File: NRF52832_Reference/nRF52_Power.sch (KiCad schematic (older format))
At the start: 37 parts, among them J17 USB_B_Micro, J18 Conn_01x02_Male, U10 DW01, U11 LMV331ICT, U12 AP2138N-3.0TRG1, U13 FS8205A, U14 SLIDE_SW_DPDT, U7 TPS613222ADBVR, U8 NCV8161BSN330T1G, U9 TP4056E-SN2L1P

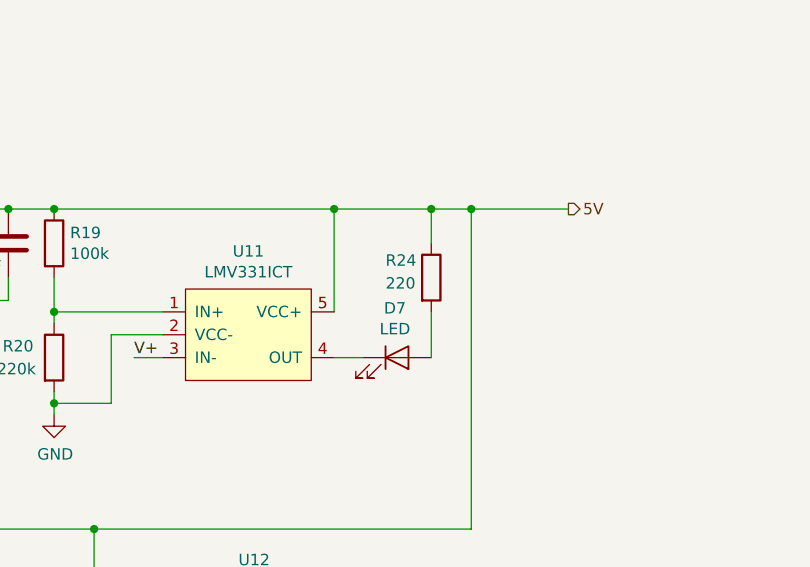
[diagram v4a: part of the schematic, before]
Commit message: Fixed wrong values for some components
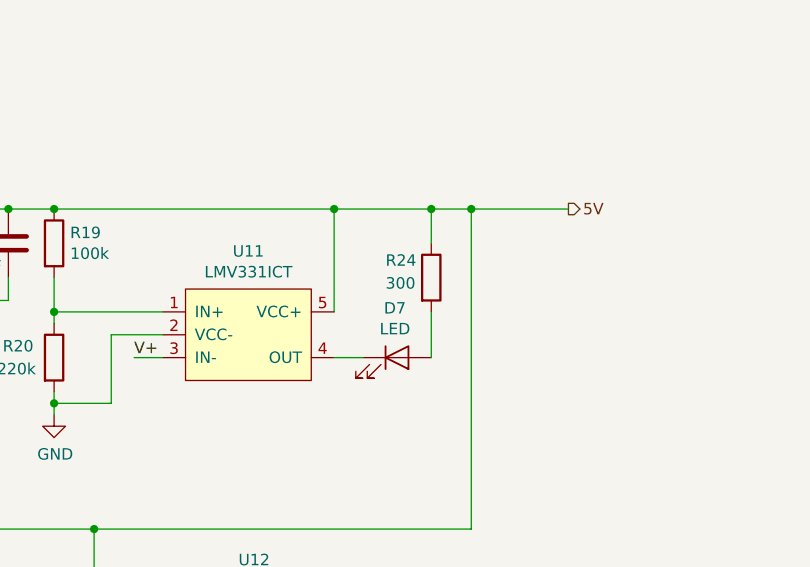
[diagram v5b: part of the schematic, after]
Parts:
- R24: value 220 -> 300
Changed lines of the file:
@@
 P 4800 5400
 F 0 "R24" H 4600 5475 50  0000 L CNN
-F 1 "220" H 4600 5375 50  0000 L CNN
+F 1 "300" H 4600 5375 50  0000 L CNN
 F 2 "Resistor_SMD:R_0603_1608Metric_Pad1.05x0.95mm_HandSolder" V 4730 5400 50  0001 C CNN
 F 3 "~" H 4800 5400 50  0001 C CNN

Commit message: Updating rescue lib for NRF52 Reference.
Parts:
- U12: symbol Project_Libary:AP2138N-3.0TRG1 -> NRF52832_Reference-rescue:AP2138N-3.0TRG1-Project_Libary
- U7: symbol Project_Libary:TPS613222ADBVR -> NRF52832_Reference-rescue:TPS613222ADBVR-Project_Libary
- U9: symbol Project_Libary:TP4056E-SN2L1P -> NRF52832_Reference-rescue:TP4056E-SN2L1P-Project_Libary
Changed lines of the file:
@@
 	3550 1300 3550 1400
 $Comp
-L Project_Libary:TP4056E-SN2L1P U9
+L NRF52832_Reference-rescue:TP4056E-SN2L1P-Project_Libary U9
 U 1 1 5BF35E0A
 P 2650 1950
@@
 $EndComp
 $Comp
-L Project_Libary:TPS613222ADBVR U?
+L NRF52832_Reference-rescue:TPS613222ADBVR-Project_Libary U?
 U 1 1 5BF5919E
 P 1850 5000
@@
 	4975 5100 4975 6500
 $Comp
-L Project_Libary:AP2138N-3.0TRG1 U12
+L NRF52832_Reference-rescue:AP2138N-3.0TRG1-Project_Libary U12
 U 1 1 5C11B1D5
 P 4025 6900
+AR Path="/5C11B1D5" Ref="U12"  Part="1"
+AR Path="/5BF31556/5C11B1D5" Ref="U12"  Part="1"
 F 0 "U12" H 4025 7165 50  0000 C CNN
 F 1 "AP2138N-3.0TRG1" H 4025 7074 50  0000 C CNN
